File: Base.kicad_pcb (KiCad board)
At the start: 2 copper layers, 154.9 x 63.5 mm, 41 parts, among them J3 ICSP, J5 CON8, J6 CON8, J7 CON8, J9 3vias, P1 CONN_01X04, P10 CONN_01X04, P4 CONN_01X04, P5 CONN_01X09, P6 USB_B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

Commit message: Bugs en PCNEW
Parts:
- moved S3 0.76 mm to (84.4, 90.3)
- moved S4 0.58 mm to (71.7, 90.3)
- moved S5 0.15 mm to (89.0, 124.5)
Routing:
- net GND: track 535.4 -> 537.0 mm
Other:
- outline, holes or cut-outs redrawn
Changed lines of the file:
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@@
     (links 235)
     (no_connects 13)
-    (area 64.225 32.969999 230.290572 148.75)
+    (area 65.989999 76.149999 221.030001 139.750001)
     (thickness 1.6)
-    (drawings 80)
-    (tracks 370)
+    (drawings 82)
+    (tracks 369)
     (zones 0)
     (modules 41)
@@
   )
   (module libreria:SW_PUSH_6mm_h13mm (layer F.Cu)
-    (at 88.955 124.31 270)
+    (at 88.955 124.46 270)
     (descr "tactile push button, 6x6mm e.g. PHAP33xx series, height=13mm")
     (tags "tact sw push 6mm")
@@
   )
   (module libreria:SW_PUSH_6mm_h13mm (layer F.Cu)
-    (at 71.12 90.32 90)
+    (at 71.7 90.32 90)
     (descr "tactile push button, 6x6mm e.g. PHAP33xx series, height=13mm")
     (tags "tact sw push 6mm")
@@
   )
   (module libreria:SW_PUSH_6mm_h13mm (layer F.Cu)
-    (at 83.82 90.805 90)
+    (at 84.4 90.32 90)
     (descr "tactile push button, 6x6mm e.g. PHAP33xx series, height=13mm")
     (tags "tact sw push 6mm")
@@
     )
   )
-  (gr_line (start 66.04 76.2) (end 220.98 76.2) (layer Edge.Cuts) (width 0.1))
+  (gr_line (start 69.85 76.2) (end 66.04 76.2) (layer Edge.Cuts) (width 0.1))
+  (gr_line (start 220.98 76.2) (end 217.17 76.2) (layer Edge.Cuts) (width 0.1))
   (dimension 154.94 (width 0.3) (layer Dwgs.User)
     (gr_text 154,940mm (at 143.51 147.399999) (layer Dwgs.User)
@@
     (arrow2b (pts (xy 66.04 146.049999) (xy 67.166504 145.463578)))
   )
+  (gr_line (start 217.17 76.2) (end 69.85 76.2) (layer Edge.Cuts) (width 0.1))
   (gr_line (start 66.04 76.2) (end 66.04 76.835) (layer Edge.Cuts) (width 0.1))
   (gr_line (start 220.98 139.7) (end 218.44 139.7) (layer Edge.Cuts) (width 0.1))
@@
   (gr_circle (center 88.9 110.49) (end 88.9 109.22) (layer Edge.Cuts) (width 0.1))
   (gr_circle (center 88.9 101.6) (end 90.17 101.6) (layer Edge.Cuts) (width 0.1))
-  (gr_circle (center 217.17 80.01) (end 217.17 78.74) (layer Edge.Cuts) (width 0.1))
+  (gr_circle (center 217.17 81.28) (end 217.17 80.01) (layer Edge.Cuts) (width 0.1))
   (gr_circle (center 217.17 135.89) (end 217.17 134.62) (layer Edge.Cuts) (width 0.1))
   (gr_circle (center 69.85 80.01) (end 69.85 78.74) (layer Edge.Cuts) (width 0.1))
@@
   (segment (start 114.935 89.535) (end 114.935 85.725) (width 0.635) (layer B.Cu) (net 11))
   (segment (start 121.92 100.33) (end 121.92 87.63) (width 0.635) (layer B.Cu) (net 11))
+  (segment (start 110.49 81.915) (end 108.585 80.01) (width 0.8) (layer B.Cu) (net 12))
+  (segment (start 108.585 80.01) (end 79.43 80.01) (width 0.8) (layer B.Cu) (net 12))
+  (segment (start 88.9 85.09) (end 88.9 83.82) (width 0.8) (layer B.Cu) (net 12))
+  (segment (start 79.43 80.01) (end 75.62 83.82) (width 0.8) (layer B.Cu) (net 12))
+  (segment (start 75.62 83.82) (end 78.16 86.36) (width 0.8) (layer B.Cu) (net 12))
+  (segment (start 78.16 86.36) (end 87.63 86.36) (width 0.8) (layer B.Cu) (net 12))
+  (segment (start 87.63 86.36) (end 88.9 85.09) (width 0.8) (layer B.Cu) (net 12))
   (segment (start 185.674 106.553) (end 187.96 104.267) (width 0.8) (layer B.Cu) (net 12))
   (segment (start 187.96 104.267) (end 187.96 100.33) (width 0.8) (layer B.Cu) (net 12))
@@
   (segment (start 112.53363 96.52) (end 112.395 96.52) (width 0.8) (layer B.Cu) (net 12))
   (segment (start 113.80363 95.25) (end 112.53363 96.52) (width 0.8) (layer B.Cu) (net 12))
-  (segment (start 79.43 80.01) (end 108.585 80.01) (width 0.8) (layer B.Cu) (net 12))
-  (segment (start 108.585 80.01) (end 110.49 81.915) (width 0.8) (layer B.Cu) (net 12))
-  (segment (start 75.62 83.82) (end 79.43 80.01) (width 0.8) (layer B.Cu) (net 12))
   (segment (start 92.072208 134.62) (end 103.502208 123.19) (width 0.8) (layer B.Cu) (net 12))
   (segment (start 103.502208 123.19) (end 106.045 123.19) (width 0.8) (layer B.Cu) (net 12))
@@
   (segment (start 71.755 104.775) (end 71.755 104.14) (width 0.8) (layer B.Cu) (net 12))
   (segment (start 75.62 90.32) (end 71.755 94.185) (width 0.8) (layer B.Cu) (net 12))
-  (segment (start 75.62 83.82) (end 78.16 86.36) (width 0.8) (layer B.Cu) (net 12))
-  (segment (start 86.265 86.36) (end 87.320001 85.304999) (width 0.8) (layer B.Cu) (net 12))
-  (segment (start 78.16 86.36) (end 86.265 86.36) (width 0.8) (layer B.Cu) (net 12))
-  (segment (start 87.320001 85.304999) (end 88.32 84.305) (width 0.8) (layer B.Cu) (net 12))
   (segment (start 111.125 128.27) (end 109.922919 128.27) (width 0.8) (layer B.Cu) (net 12))
   (segment (start 109.922919 128.27) (end 108.585 126.932081) (width 0.8) (layer B.Cu) (net 12))
@@
   (segment (start 107.315 92.075) (end 104.14 95.25) (width 0.635) (layer B.Cu) (net 33))
   (segment (start 104.14 95.25) (end 100.965 95.25) (width 0.635) (layer B.Cu) (net 33))
-  (segment (start 83.82 90.805) (end 83.82 89.916) (width 0.635) (layer B.Cu) (net 34))
-  (segment (start 83.82 89.916) (end 85.09 88.646) (width 0.635) (layer B.Cu) (net 34))
-  (segment (start 85.09 88.646) (end 91.7194 88.646) (width 0.635) (layer B.Cu) (net 34))
-  (segment (start 91.7194 88.646) (end 92.71 89.6366) (width 0.635) (layer B.Cu) (net 34))
-  (segment (start 92.71 89.6366) (end 92.71 90.805) (width 0.635) (layer B.Cu) (net 34))
-  (segment (start 83.185 95.25) (end 83.185 91.44) (width 0.635) (layer B.Cu) (net 34))
-  (segment (start 83.185 91.44) (end 83.82 90.805) (width 0.635) (layer B.Cu) (net 34))
+  (segment (start 83.185 95.25) (end 83.185 91.535) (width 0.635) (layer B.Cu) (net 34))
+  (segment (start 83.185 91.535) (end 84.4 90.32) (width 0.635) (layer B.Cu) (net 34))
+  (segment (start 92.71 90.805) (end 92.71 89.6366) (width 0.635) (layer B.Cu) (net 34))
+  (segment (start 92.71 89.6366) (end 91.3384 88.265) (width 0.635) (layer B.Cu) (net 34))
+  (segment (start 91.3384 88.265) (end 86.455 88.265) (width 0.635) (layer B.Cu) (net 34))
+  (segment (start 86.455 88.265) (end 84.4 90.32) (width 0.635) (layer B.Cu) (net 34))
   (segment (start 71.12 83.82) (end 71.755 83.82) (width 0.635) (layer B.Cu) (net 35))
   (segment (start 71.755 83.82) (end 75.692 87.757) (width 0.635) (layer B.Cu) (net 35))

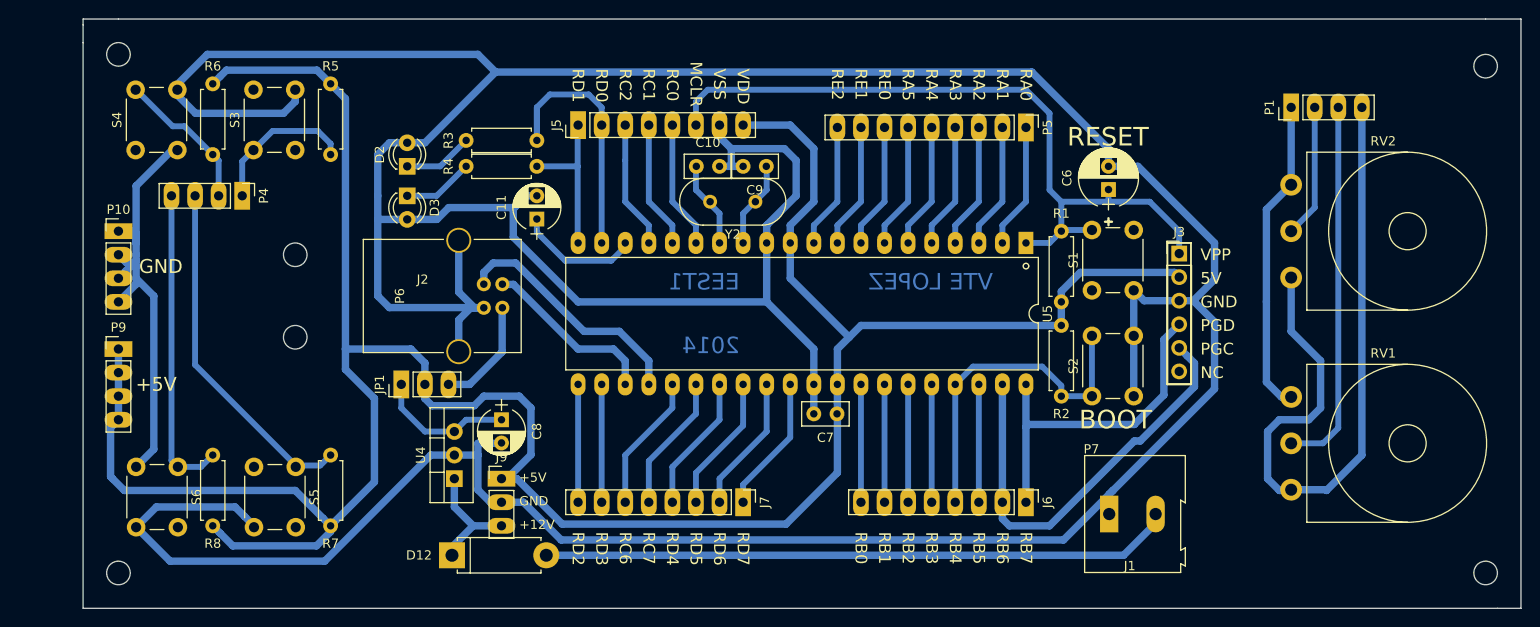
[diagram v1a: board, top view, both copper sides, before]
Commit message: Diseño definitivo con desplazamiento USB
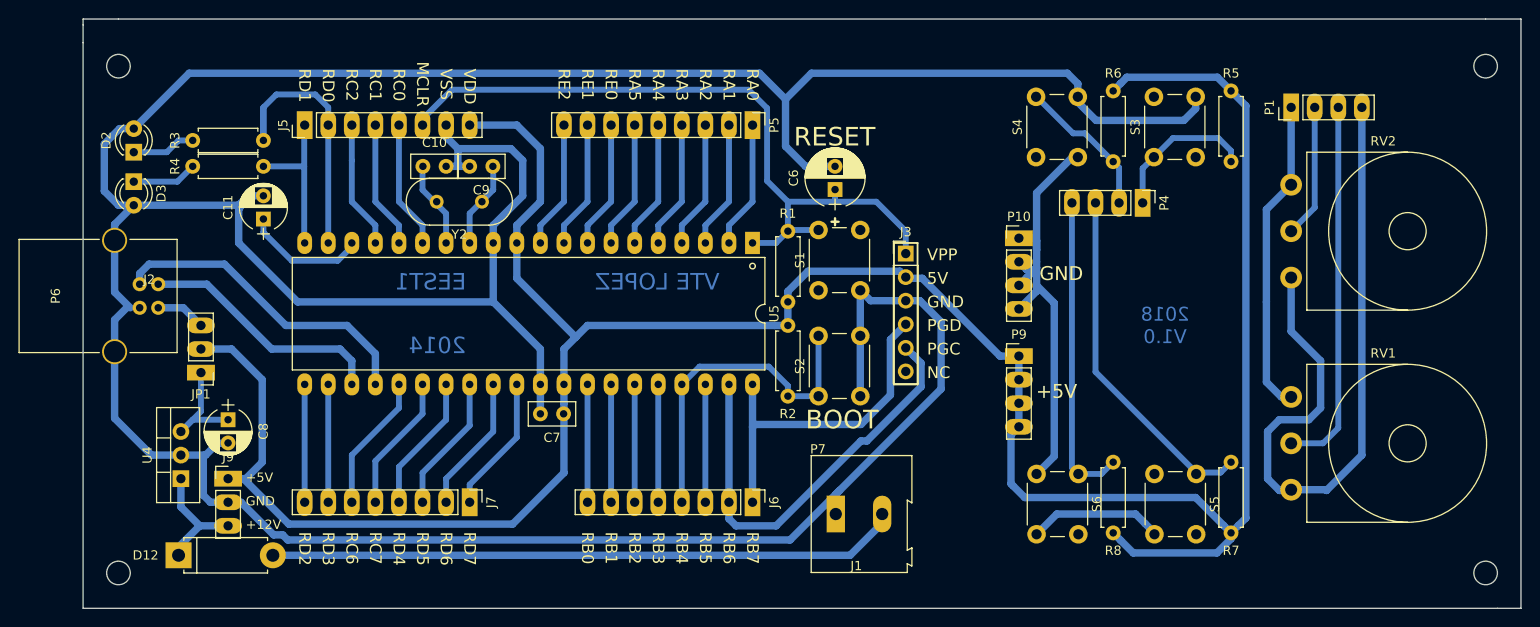
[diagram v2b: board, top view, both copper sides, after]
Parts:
- P6: footprint libreria:USB_B -> USB_B
- moved R5 97.0 mm to (189.7, 83.9)
- moved R6 97.0 mm to (177.0, 83.9)
- moved R7 97.0 mm to (189.7, 131.6)
- moved R8 97.0 mm to (177.0, 131.6)
- moved S4 97.0 mm to (168.7, 91.1)
- moved S5 97.0 mm to (186.0, 125.2)
- moved P10 97.0 mm to (166.9, 99.8)
- moved P4 97.0 mm to (180.2, 96.0)
- moved P9 97.0 mm to (166.9, 112.5)
- moved S3 97.0 mm to (181.4, 91.1)
- moved S6 97.0 mm to (173.3, 125.2)
- moved P6 37.1 mm to (74.1, 107.3)
- moved D2 29.5 mm to (71.5, 90.6)
- moved D3 29.5 mm to (71.5, 93.7)
- moved P5 29.5 mm to (138.2, 87.6)
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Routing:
- net GND: track 537.0 -> 470.1 mm
- net RC5: track 26.4 -> 34.3 mm
- net RC4: track 19.2 -> 26.8 mm
- net +5VUSB: track 12.0 -> 5.39 mm
- net Net-(C8-Pad1): track 14.9 -> 12.9 mm
- net MCRL: track 81.0 -> 79.6 mm
- net Net-(D2-Pad1): track 7.51 -> 6.88 mm
- net Net-(D3-Pad1): track 7.67 -> 7.03 mm
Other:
- outline, holes or cut-outs redrawn
- board text added: "2018 V1.0"
